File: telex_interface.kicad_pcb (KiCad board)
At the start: 4 copper layers, 61 x 52.3 mm, 49 parts, among them J1 DB25_Female_MountingHoles, J2 Conn_02x08_Odd_Even, J3 USB_B_Mini, J4 Raspberry_Pi_2_3, U1 max3387, U2 74LVC1G08, U3 CH340G, Y1 EuroQuartz MJ 5x3.2mm 12MHz

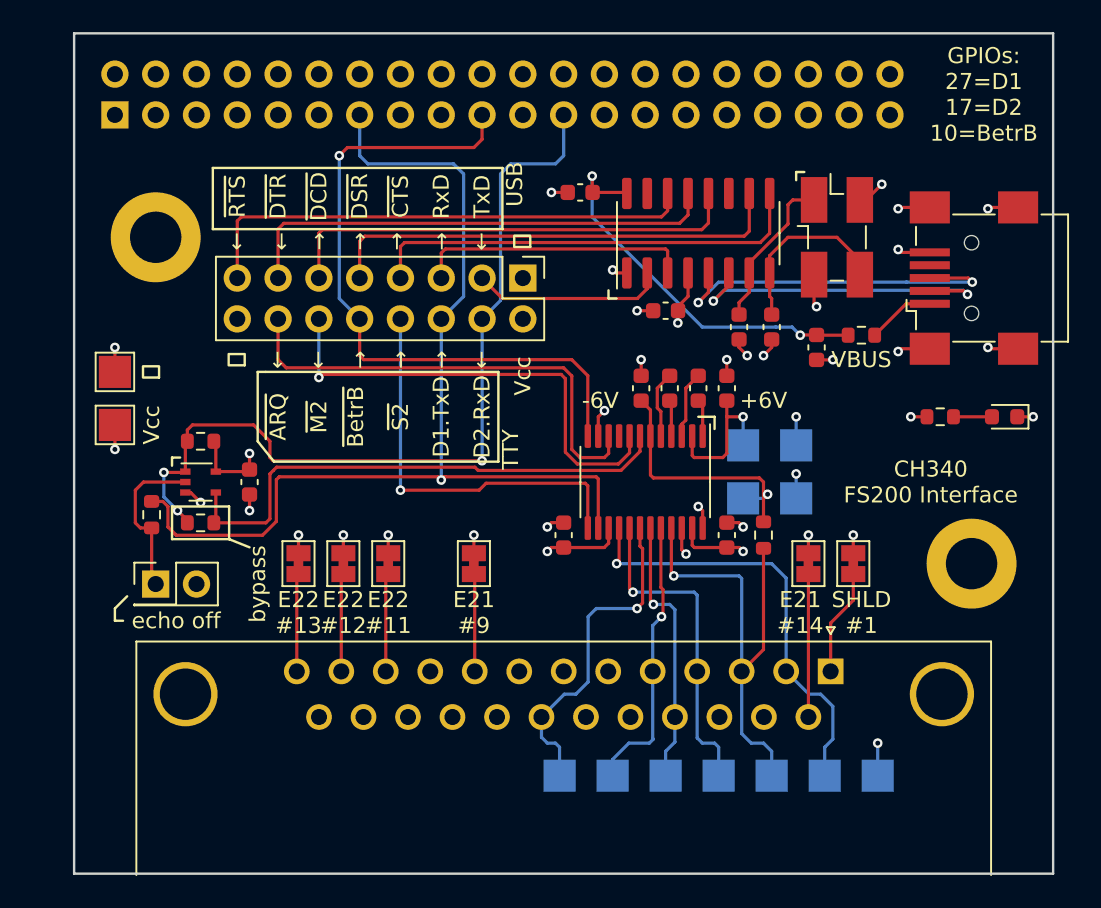
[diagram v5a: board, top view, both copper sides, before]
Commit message: removed USB again, made smaller
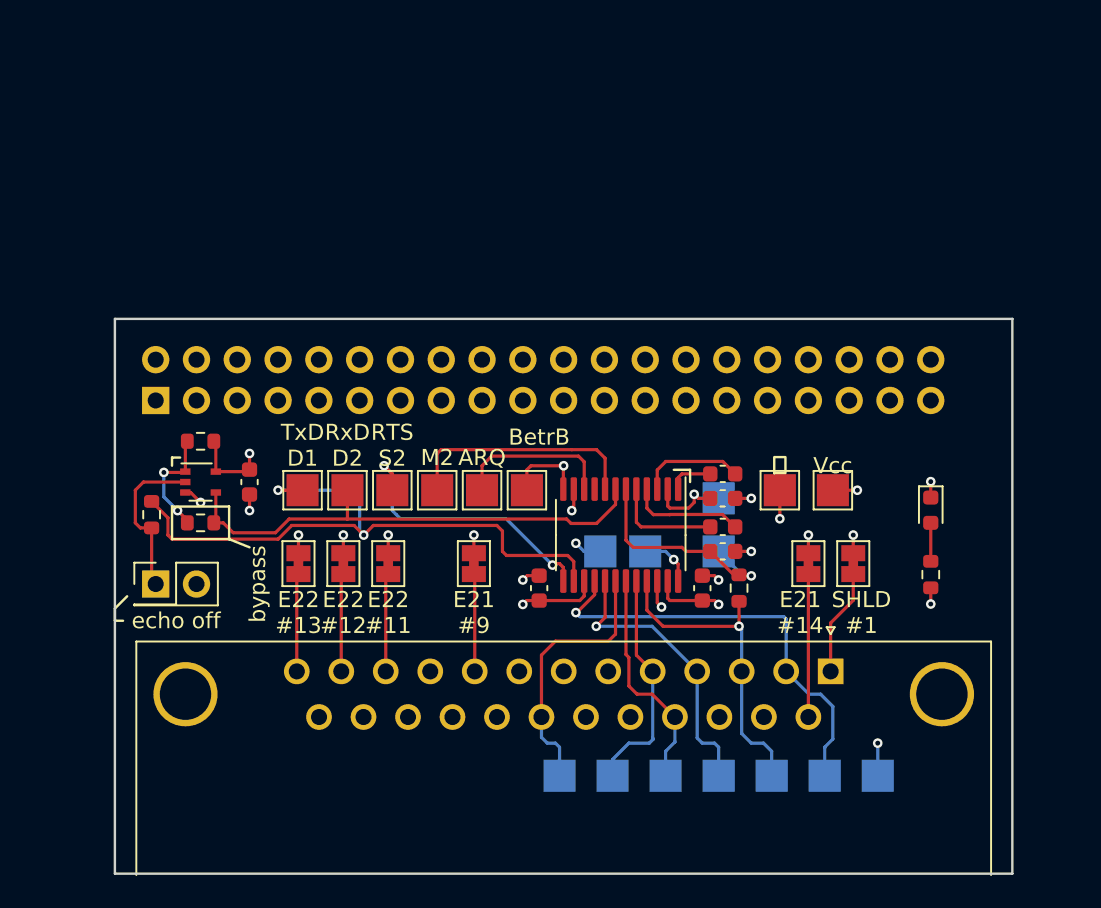
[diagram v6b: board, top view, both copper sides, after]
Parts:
- removed C10, C9: 100n, Capacitor_SMD:C_0603_1608Metric
- removed C11, C12: 22p, Capacitor_SMD:C_0603_1608Metric
- removed C8: 10u, Capacitor_SMD:C_0603_1608Metric
- removed H1, H2: MountingHole_Pad, MountingHole:MountingHole_3.2mm_M3_DIN965_Pad
- removed J2: Conn_02x08_Odd_Even, Connector_PinHeader_2.54mm:PinHeader_2x08_P2.54mm_Vertical
- removed J3: USB_B_Mini, Connector_USB:USB_Mini-B_Wuerth_65100516121_Horizontal
- removed R7: 22R, Resistor_SMD:R_0603_1608Metric
- removed U3: CH340G, Package_SO:SOIC-16_3.9x9.9mm_P1.27mm
- removed Y1: EuroQuartz MJ 5x3.2mm 12MHz, Crystal:Crystal_SMD_EuroQuartz_MJ-4Pin_5.0x3.2mm_HandSoldering
- added TP14: TestPoint, TestPoint:TestPoint_Pad_2.0x2.0mm, F.Cu at (164.3, 107.2)
- added TP15: TestPoint, TestPoint:TestPoint_Pad_2.0x2.0mm, F.Cu at (169.9, 107.2)
- added TP16: TestPoint, TestPoint:TestPoint_Pad_2.0x2.0mm, F.Cu at (172.7, 107.2)
- added TP17: TestPoint, TestPoint:TestPoint_Pad_2.0x2.0mm, F.Cu at (161.5, 107.2)
- added TP18: TestPoint, TestPoint:TestPoint_Pad_2.0x2.0mm, F.Cu at (167.1, 107.2)
- added TP19: TestPoint, TestPoint:TestPoint_Pad_2.0x2.0mm, F.Cu at (175.5, 107.2)
- moved TP13 44.9 mm to (194.6, 107.2), turned to 90 degrees
- moved TP12 42.1 mm to (191.3, 107.2), turned to 90 degrees
- moved J4 18.0 mm to (152.4, 101.6)
- moved TP11 13.9 mm to (180.1, 111.0)
- moved C3 11.4 mm to (187.7, 111.0), turned to 0 degrees
- moved TP9 9.96 mm to (182.9, 111.0)
- moved R4 9.84 mm to (200.7, 112.4), turned to -90 degrees
- moved C5 9.25 mm to (187.7, 109.5), turned to 180 degrees
- moved D1 7.41 mm to (200.7, 108.4), turned to -90 degrees
- moved C2 6.86 mm to (187.7, 107.7), turned to 180 degrees
- moved C4 5.55 mm to (187.7, 106.2), turned to 0 degrees
- moved C1 3.64 mm to (186.4, 113.3)
- moved C6 3.64 mm to (176.3, 113.3)
- moved R1 3.64 mm to (188.7, 113.3)
- moved TP8 3.64 mm to (187.5, 111.0)
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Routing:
- net /RxD_PC: track 52.6 -> 6.64 mm, vias 3 -> 2
- net /~{BetrB_DTR}: track 42.3 -> 5.12 mm
- net /~{USB_RTS}: track 31.7 -> 0.00 mm
- net /~{USB_DTR}: track 30.3 -> 0.00 mm
- net /~{USB_DCD}: track 29.2 -> 0.00 mm
- net /~{USB_DSR}: track 29.2 -> 0.00 mm
- net /~{USB_CTS}: track 27.8 -> 0.00 mm
- net VBUS: track 24.6 -> 0.00 mm, vias 2 -> 0
- net /TxD: track 64.9 -> 41.1 mm, vias 1 -> 2
- net /USB_DP: track 22.4 -> 0.00 mm, vias 2 -> 0
- net /USB_DN: track 20.8 -> 0.00 mm, vias 2 -> 0
- net GND: track 41.5 -> 21.5 mm, vias 30 -> 17
- net /~{ARQ}: track 29.5 -> 9.98 mm
- net /USB_RxD: track 17.2 -> 0.00 mm
- net /~{M2}: track 29.4 -> 15.0 mm, vias 1 -> 0
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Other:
- board size 61 x 52.3 mm -> 55.9 x 34.5 mm
- board text added: "BetrB"
- board text added: "RTS S2"
- board text added: "RxD D2"
- board text added: "TxD D1"
- board text removed: "CH340 FS200 Interface"
- board text removed: "D1.TxD"
- board text removed: "D2.RxD"
- board text removed: "GPIOs: 27=D1 17=D2 10=BetrB"
- board text removed: "RxD"
- board text removed: "TTY"
- board text removed: "TxD"
- board text removed: "USB"
- board text removed: "USB_DN"
- board text removed: "USB_DP"
- board text removed: "VBUS"
- board text removed: "~{ARQ}"
- board text removed: "~{BetrB}"
- board text removed: "~{CTS}"
- board text removed: "~{DCD}"
- board text removed: "~{DSR}"
- board text removed: "~{DTR}"
- board text removed: "~{M2}"
- board text removed: "~{RTS}"
- board text removed: "~{S2}"
- board text removed: "→"

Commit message: moar work
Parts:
- removed J4: Raspberry_Pi_2_3, Connector_PinSocket_2.54mm:PinSocket_2x20_P2.54mm_Vertical
- added J2: Conn_02x20_Odd_Even, Connector_PinSocket_2.54mm:PinSocket_2x20_P2.54mm_Vertical, B.Cu at (152.4, 101.6)
- added JP10: SolderJumper_2_Bridged, Jumper:SolderJumper-2_P1.3mm_Bridged_Pad1.0x1.5mm, B.Cu at (175.0, 105.2)
- added JP11: SolderJumper_2_Open, Jumper:SolderJumper-2_P1.3mm_Open_Pad1.0x1.5mm, B.Cu at (177.8, 105.2)
- added JP12: SolderJumper_2_Open, Jumper:SolderJumper-2_P1.3mm_Open_Pad1.0x1.5mm, B.Cu at (171.2, 105.2)
- added JP13: SolderJumper_2_Open, Jumper:SolderJumper-2_P1.3mm_Open_Pad1.0x1.5mm, B.Cu at (180.6, 105.2)
- added JP8: SolderJumper_2_Bridged, Jumper:SolderJumper-2_P1.3mm_Bridged_Pad1.0x1.5mm, B.Cu at (165.1, 105.2)
- added JP9: SolderJumper_2_Bridged, Jumper:SolderJumper-2_P1.3mm_Bridged_Pad1.0x1.5mm, B.Cu at (168.1, 105.2)
- added TP20: TestPoint, TestPoint:TestPoint_Pad_2.0x2.0mm, B.Cu at (174.5, 125.0)
- added TP21: TestPoint, TestPoint:TestPoint_Pad_2.0x2.0mm, B.Cu at (171.4, 125.0)
- added TP22: TestPoint, TestPoint:TestPoint_Pad_2.0x2.0mm, F.Cu at (203.2, 107.2)
- added TP23: TestPoint, TestPoint:TestPoint_Pad_2.0x2.0mm, F.Cu at (199.9, 107.2)
- moved D1 6.79 mm to (203.0, 114.8), turned to 180 degrees
- moved R4 2.55 mm to (199.7, 114.8), turned to 180 degrees
- moved TP9 0.25 mm to (183.1, 111.0)
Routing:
- net /GPIO1_Rx2: track 0.00 -> 24.1 mm
- net /GPIO0_Tx3: track 0.00 -> 23.1 mm
- net /RxD_TTY: track 30.7 -> 39.1 mm, vias 0 -> 1
- net /~{BetrB_DTR}: track 5.12 -> 10.0 mm
- net /TxD: track 41.1 -> 37.6 mm, vias 2 -> 1
- net /~{S2_RTS}: track 17.8 -> 21.3 mm, vias 2 -> 3
- net /GPIO22: track 0.00 -> 3.33 mm
- net /~{ARQ}: track 9.98 -> 13.1 mm, vias 0 -> 1
- net /GPIO27: track 0.00 -> 3.12 mm
- net /GPIO10: track 0.00 -> 3.01 mm
- net /GPIO17: track 0.00 -> 2.91 mm
- net GND: track 21.5 -> 24.4 mm, vias 17 -> 18
- net /~{M2}: track 15.0 -> 17.8 mm, vias 0 -> 1
- net /GPIO9: track 0.00 -> 2.40 mm
- net /GPIO11: track 0.00 -> 2.40 mm
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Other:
- board text added: "3.3V"
- board text added: "IO0 Tx2"
- board text added: "IO1 Rx2"
- board text added: "IO10 S2"
- board text added: "IO11 ARQ"
- board text added: "IO17 D1 TxD"
- board text added: "IO22 Betr"
- board text added: "IO27 D2 RxD"
- board text added: "IO9 M2"
- board text added: "RPi4 uart2"
- board text added: "← Raspi GPIO ← V10 Signal"
- board text removed: "bypass"

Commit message: Further work...
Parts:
- removed TP22, TP23: TestPoint, TestPoint:TestPoint_Pad_2.0x2.0mm
- added H1: MountingHole, MountingHole:MountingHole_2.7mm_M2.5, F.Cu at (147.5, 100.3)
- added H2: MountingHole, MountingHole:MountingHole_2.7mm_M2.5, F.Cu at (205.5, 100.3)
- added J3: Conn_01x03_Male, Connector_PinHeader_2.54mm:PinHeader_1x03_P2.54mm_Vertical, F.Cu at (147.6, 107.4)
- added J4: Conn_02x04_Odd_Even, Connector_PinHeader_2.54mm:PinHeader_2x04_P2.54mm_Vertical, F.Cu at (206.3, 113.8)
- added TP24: TestPoint, TestPoint:TestPoint_Pad_2.0x2.0mm, B.Cu at (160.3, 105.2)
- added TP25: TestPoint, TestPoint:TestPoint_Pad_2.0x2.0mm, B.Cu at (156.2, 105.2)
- added TP26: TestPoint, TestPoint:TestPoint_Pad_2.0x2.0mm, B.Cu at (158.2, 110.7)
- moved R4 15.2 mm to (206.0, 128.7), turned to -90 degrees
- moved D1 11.0 mm to (206.0, 125.4), turned to -90 degrees
- moved TP21 5.59 mm to (177.0, 124.7)
- moved TP20 4.06 mm to (170.4, 124.7)
- moved TP6 3.82 mm to (173.7, 124.7)
- moved J1 1.28 mm to (193.2, 118.5)
- moved TP10 0.57 mm to (196.8, 124.7)
- moved TP2 0.57 mm to (180.3, 124.7)
- moved TP3 0.57 mm to (183.6, 124.7)
- moved TP4 0.57 mm to (193.5, 124.7)
- moved TP5 0.57 mm to (186.9, 124.7)
- moved TP1 0.57 mm to (190.2, 124.7)
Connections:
- net Net-(C4-Pad1) renamed /C1pos
- net Net-(C4-Pad2) renamed /C1neg
- net Net-(C5-Pad1) renamed /C2pos
- net Net-(C5-Pad2) renamed /C2neg
- J2 pad 10: unconnected-(J2-Pad10) -> /GPIO15_Cons_Rx
- J2 pad 12: unconnected-(J2-Pad12) -> /GPIO18_CE0
- J2 pad 27: /GPIO0_Tx3 -> unconnected-(J2-Pad27)
- J2 pad 28: /GPIO1_Rx2 -> unconnected-(J2-Pad28)
- J2 pad 3: unconnected-(J2-Pad3) -> /GPIO2_SDA
- J2 pad 35: unconnected-(J2-Pad35) -> /GPIO19_CIPO
- J2 pad 36: unconnected-(J2-Pad36) -> /GPIO16_CE2
- J2 pad 38: unconnected-(J2-Pad38) -> /GPIO20_COPI
- J2 pad 40: unconnected-(J2-Pad40) -> /GPIO21_SCLK
- J2 pad 5: unconnected-(J2-Pad5) -> /GPIO3_SCL
- J2 pad 8: unconnected-(J2-Pad8) -> /GPIO14_Cons_Tx
- U1 pad 16: V10_D1_TxD -> V10_BetrB_DTR
- U1 pad 18: V10_BetrB_DTR -> V10_D1_TxD
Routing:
- net /GPIO18_CE0: track 0.00 -> 47.6 mm, vias 0 -> 1
- net /GPIO15_Cons_Rx: track 0.00 -> 32.1 mm
- net /GPIO14_Cons_Tx: track 0.00 -> 24.5 mm
- net /GPIO1_Rx2: track 24.1 -> 0.00 mm
- net /GPIO0_Tx3: track 23.1 -> 0.00 mm
- net GND: track 24.4 -> 43.5 mm, vias 18 -> 16
- net /GPIO19_CIPO: track 0.00 -> 17.8 mm
- net /GPIO21_SCLK: track 0.00 -> 17.5 mm
- net /GPIO16_CE2: track 0.00 -> 15.4 mm
- net /GPIO20_COPI: track 0.00 -> 13.1 mm
- net /GPIO3_SCL: track 0.00 -> 5.16 mm
- net /GPIO2_SDA: track 0.00 -> 4.08 mm
- net V10_D1_TxD: track 27.3 -> 23.6 mm
- net /SHIELD@1: track 6.64 -> 8.53 mm
- net V10_D2_RxD: track 20.1 -> 21.9 mm, vias 1 -> 0
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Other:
- board size 55.9 x 34.5 mm -> 63.5 x 34.5 mm
- board text added: "Linux Console ⏚ Tx Rx"
- board text added: "Rx2"
- board text added: "SCL"
- board text added: "SDA"
- board text added: "ce0 cipo sclk ⏚"
- board text added: "ce2 copi ⏚ Vcc"
- board text added: "spi1→"
- board text removed: "IO0 Tx2"
- board text removed: "IO1 Rx2"
- board text removed: "RPi4 uart2"
